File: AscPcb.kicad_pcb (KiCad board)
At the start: 2 copper layers, 36 parts, among them J1 12402012E212A, J2 B2B-PH-K-S, J3 Conn_01x10_Pin, SW1 RESET, SW1 TL3305AF260QG, SW2 BOOT, SW2 TL3305AF260QG, U1 ESP32-C3-WROOM-02-N4, U2 BQ24040DSQR, U3 TLV75801PDRVR

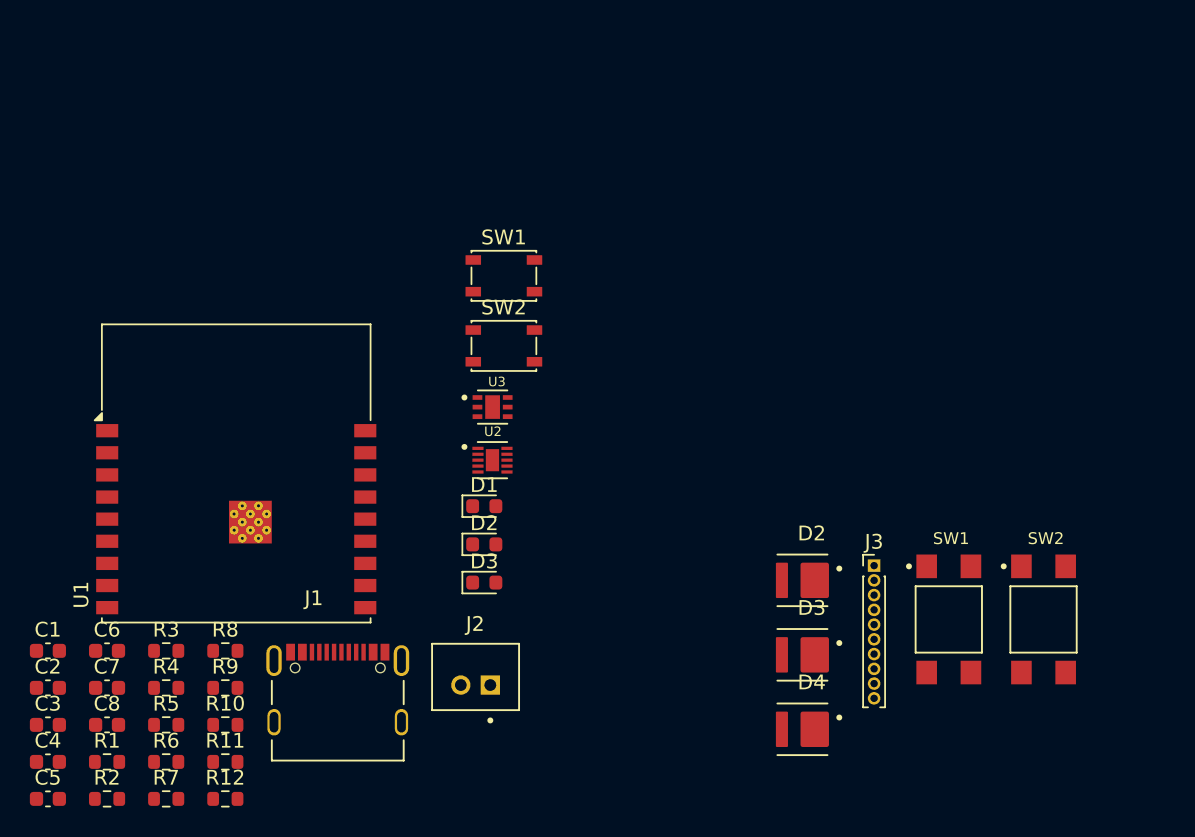
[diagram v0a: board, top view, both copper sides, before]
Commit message: sub circuits put together
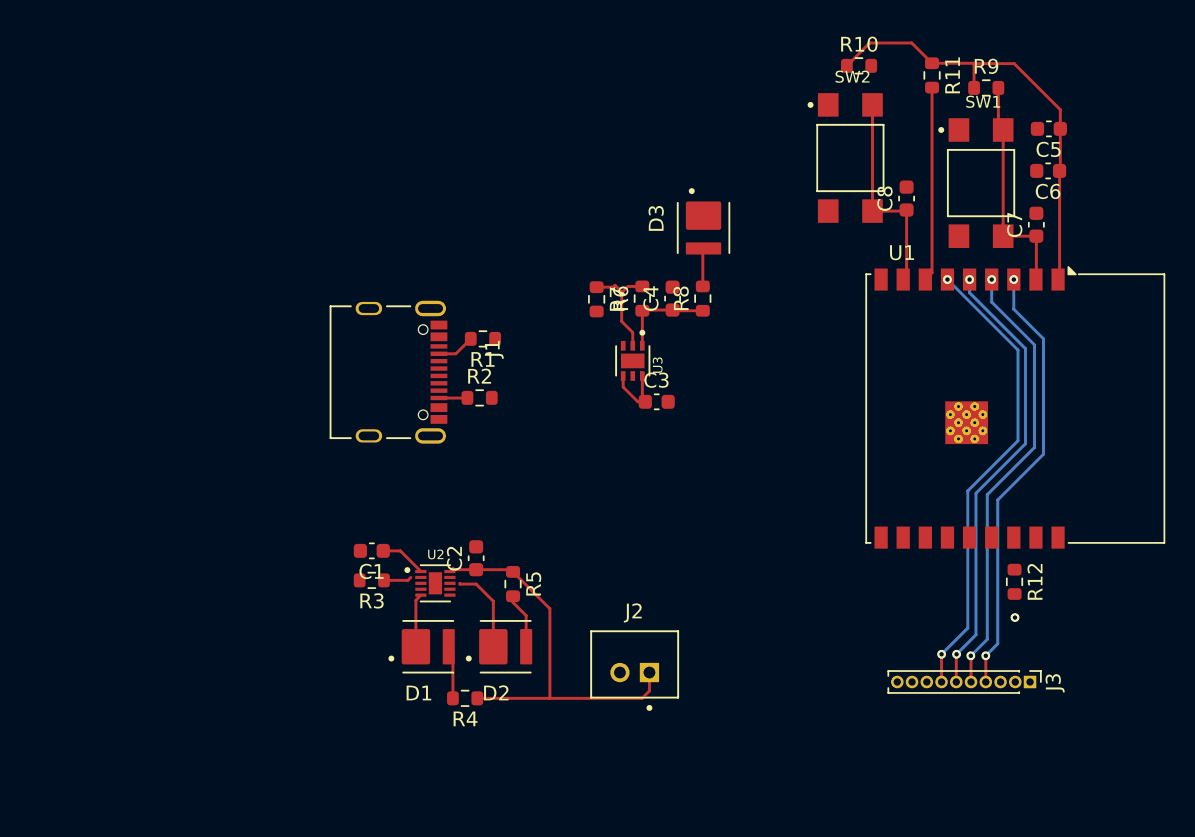
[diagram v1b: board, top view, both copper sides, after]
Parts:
- removed the D2 at (171.7, 106.9)
- removed the D2 at (150.1, 104.5)
- removed the D3 at (150.1, 107.0)
- removed the D3 at (171.7, 112.0)
- removed D4: Green, L135_G525003500000:LED_L135-G525003500000
- removed the SW1 at (151.4, 86.2)
- removed the SW1 at (181.6, 109.5)
- removed the SW2 at (151.4, 91.0)
- removed the SW2 at (188.0, 109.5)
- added D2: RED, L135_G525003500000:LED_L135-G525003500000, F.Cu at (151.5, 111.4)
- added D3: Green, L135_G525003500000:LED_L135-G525003500000, F.Cu at (165.0, 83.0)
- added SW1: TL3305AF260QG, TL3305AF260QG:SW_TL3305AF260QG, F.Cu at (183.8, 80.0)
- added SW2: TL3305AF260QG, TL3305AF260QG:SW_TL3305AF260QG, F.Cu at (174.9, 78.3)
- D1: footprint LED_SMD:LED_0603_1608Metric -> L135_G525003500000:LED_L135-G525003500000
- moved C5 81.7 mm to (188.4, 76.3), turned to 180 degrees
- moved C6 71.6 mm to (188.3, 79.1), turned to 180 degrees
- moved C7 70.4 mm to (187.5, 82.8), turned to 90 degrees
- moved R11 66.8 mm to (180.5, 72.7), turned to -90 degrees
- moved R9 65.7 mm to (184.1, 73.5)
- moved C8 64.9 mm to (178.7, 81.0), turned to 90 degrees
- moved R10 62.0 mm to (175.5, 72.0)
- moved R12 55.5 mm to (186.1, 107.0), turned to -90 degrees
- moved C4 52.7 mm to (162.9, 87.8), turned to 90 degrees
- moved U1 50.3 mm to (183.0, 95.2), turned to -90 degrees
- moved C3 46.7 mm to (161.8, 94.8)
- moved R6 45.1 mm to (160.8, 87.8), turned to 90 degrees
- moved R7 44.7 mm to (157.7, 87.8), turned to -90 degrees
- moved R8 40.2 mm to (164.9, 87.8), turned to 90 degrees
- moved R1 38.4 mm to (150.0, 90.5), turned to 180 degrees
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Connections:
- J3 pad 10: IO21 -> IO10
- J3 pad 8: IO10 -> IO21
- R4 pad 2: Net-(D4-PadA) -> Net-(D1-PadA)
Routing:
- net +3V3: track 0.00 -> 36.7 mm
- net POWER: track 0.00 -> 31.8 mm
- net IO7: track 0.00 -> 31.4 mm, vias 0 -> 2
- net IO6: track 0.00 -> 30.8 mm, vias 0 -> 2
- net IO5: track 0.00 -> 30.4 mm, vias 0 -> 2
- net IO4: track 0.00 -> 29.7 mm, vias 0 -> 2
- net Net-(U1-EN): track 0.00 -> 15.4 mm
- net Net-(U1-IO9): track 0.00 -> 14.4 mm
- net Net-(U1-IO8): track 0.00 -> 13.2 mm
- net Net-(U3-FB): track 0.00 -> 7.45 mm
- net Net-(U2-~{CHG}): track 0.00 -> 5.88 mm
- net Net-(D2-PadA): track 0.00 -> 3.79 mm
- net Net-(U2-~{PG}): track 0.00 -> 3.63 mm
- net Net-(D1-PadA): track 0.00 -> 3.62 mm
- net +5V: track 0.00 -> 3.13 mm
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
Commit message: connecting some more stuff
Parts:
- moved J2 1.19 mm to (161.5, 112.6)
- moved C2 1.19 mm to (150.7, 105.4)
- moved D1 1.19 mm to (147.5, 111.4)
- moved D2 1.19 mm to (152.7, 111.4)
- moved R4 1.19 mm to (150.0, 114.9)
- moved R5 1.19 mm to (153.2, 107.1)
- moved U2 1.19 mm to (148.0, 107.1)
- moved C1 1.19 mm to (143.7, 104.9)
- moved R3 1.19 mm to (143.7, 106.9)
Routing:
- net +3V3: track 36.7 -> 103.0 mm, vias 0 -> 2
- net D+: track 0.00 -> 50.4 mm, vias 0 -> 2
- net D-: track 0.00 -> 45.2 mm, vias 0 -> 3
- net IO0: track 0.00 -> 10.6 mm
- net IO1: track 0.00 -> 10.4 mm
- net IO10: track 0.00 -> 10.2 mm
- net IO20: track 0.00 -> 10.0 mm
- net IO21: track 0.00 -> 9.83 mm
- net Net-(U1-IO9): track 14.4 -> 17.0 mm
- net Net-(U1-IO2): track 0.00 -> 2.20 mm
- net (no net): vias 1 -> 0
- added copper zone on B.Cu, net GND
- added copper zone on F.Cu, net GND
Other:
- board outline added: 49.4 x 47.9 mm

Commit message: bad but working version of pcb
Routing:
- net +5V: track 3.13 -> 35.9 mm, vias 0 -> 2
- net POWER: track 31.8 -> 46.5 mm
- net GND: vias 0 -> 46

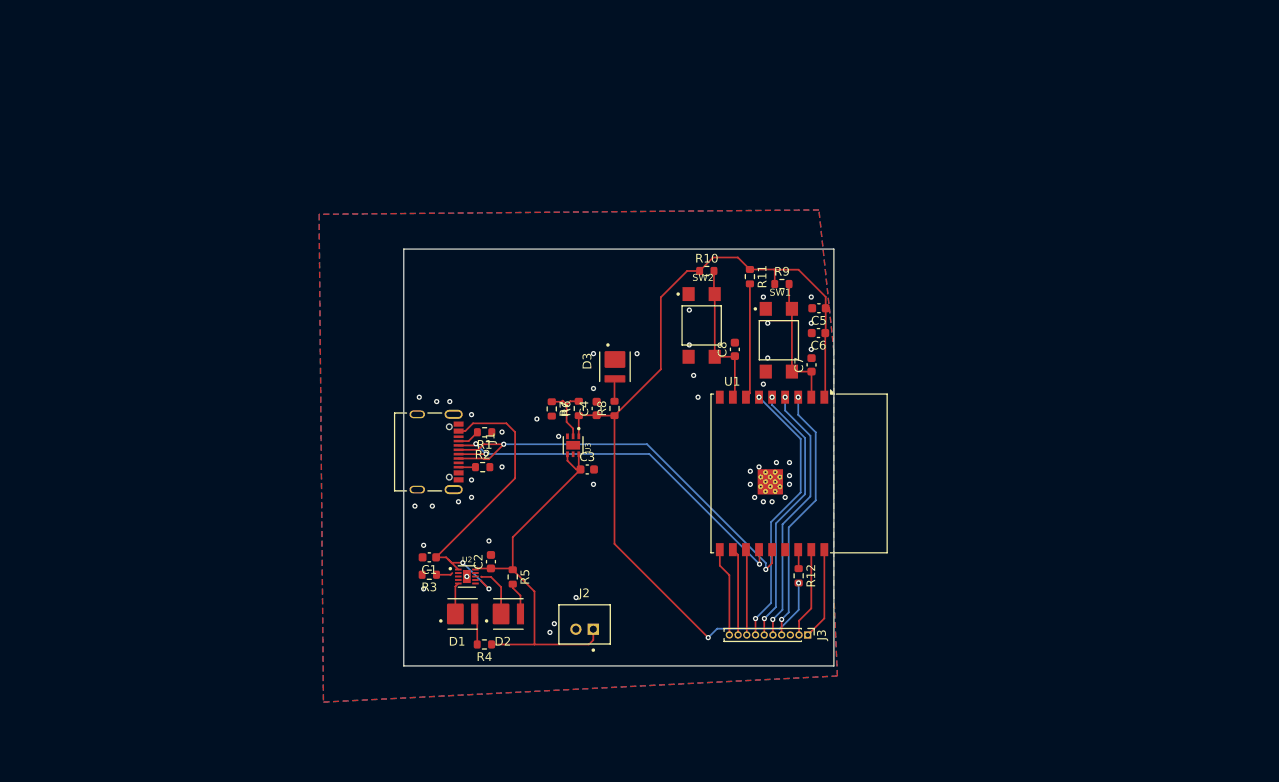
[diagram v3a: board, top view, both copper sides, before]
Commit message: new design: all components placed
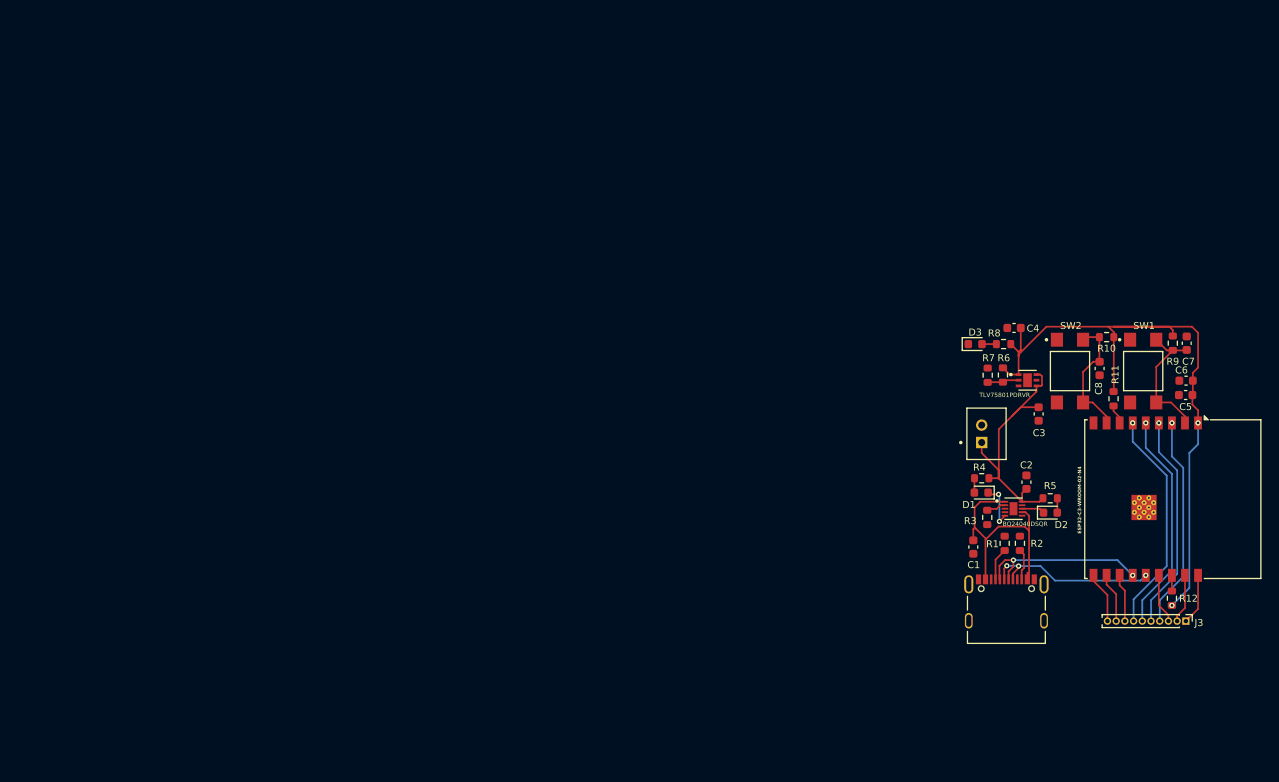
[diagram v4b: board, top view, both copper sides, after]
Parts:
- D1, D3: value Green -> GREEN; footprint L135_G525003500000:LED_L135-G525003500000 -> LED_SMD:LED_0603_1608Metric
- D2: footprint L135_G525003500000:LED_L135-G525003500000 -> LED_SMD:LED_0603_1608Metric
- J2: value B2B-PH-K-S -> B2B-PH-K-S(LF)(SN)
- R4, R5, R8: value 30 -> 150
- moved J1 70.4 mm to (209.9, 112.2), turned to 0 degrees
- moved R3 64.4 mm to (207.7, 100.3), turned to -90 degrees
- moved D2 63.3 mm to (214.9, 99.8), turned to 0 degrees
- moved U2 63.2 mm to (210.7, 99.3)
- moved C1 62.5 mm to (206.1, 103.7), turned to -90 degrees
- moved R5 62.4 mm to (214.9, 98.1), turned to 0 degrees
- moved R2 62.3 mm to (211.4, 103.3), turned to 90 degrees
- moved C2 62.1 mm to (212.2, 96.2)
- moved D1 61.1 mm to (207.0, 97.5)
- moved R1 61.0 mm to (209.7, 103.3), turned to -90 degrees
- moved R4 60.2 mm to (207.1, 95.8)
- moved U3 52.7 mm to (212.3, 84.5), turned to 0 degrees
- moved C3 52.2 mm to (213.6, 88.4), turned to -90 degrees
- moved J2 51.1 mm to (207.6, 90.7), turned to -90 degrees
- moved R7 50.2 mm to (207.8, 84.0), turned to 90 degrees
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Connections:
- R4 pad 2: Net-(D1-PadA) -> Net-(D1-A)
- R5 pad 2: Net-(D2-PadA) -> Net-(D2-A)
- R8 pad 2: Net-(D3-PadA) -> Net-(D3-A)
- U2 pad 5: Net-(U2-~{PG}) -> Net-(D1-K)
- U2 pad 8: Net-(U2-~{CHG}) -> Net-(D2-K)
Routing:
- net D+: track 50.4 -> 20.4 mm, vias 2 -> 3
- net D-: track 45.2 -> 20.3 mm, vias 3 -> 2
- net +3V3: track 103.0 -> 79.6 mm
- net POWER: track 46.5 -> 32.3 mm
- net Net-(U1-IO8): track 13.2 -> 2.24 mm
- net +5V: track 35.9 -> 29.0 mm, vias 2 -> 0
- net Net-(U2-~{CHG}): track 5.88 -> 0.00 mm
- net IO3: track 0.00 -> 5.71 mm
- net IO5: track 30.4 -> 24.9 mm, vias 2 -> 1
- net IO7: track 31.4 -> 25.9 mm, vias 2 -> 1
- net IO6: track 30.8 -> 25.4 mm, vias 2 -> 1
- net Net-(D1-K): track 0.00 -> 5.38 mm, vias 0 -> 2
- net IO4: track 29.7 -> 24.4 mm, vias 2 -> 1
- net IO1: track 10.4 -> 5.62 mm
- net IO0: track 10.6 -> 5.83 mm
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- removed copper zone on B.Cu, net GND
- removed copper zone on F.Cu, net GND
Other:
- board outline removed

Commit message: new version of pcb done
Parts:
- moved C6 82.0 mm to (149.7, 98.4)
- moved J1 82.0 mm to (129.1, 126.0)
- moved J2 82.0 mm to (126.8, 104.5)
- moved J3 82.0 mm to (149.7, 126.0)
- moved R10 82.0 mm to (140.6, 93.4)
- moved R12 82.0 mm to (148.1, 123.4)
- moved R5 82.0 mm to (134.1, 111.9)
- moved R6 82.0 mm to (128.7, 97.8)
- moved R9 82.0 mm to (148.2, 94.1)
- moved U1 82.0 mm to (145.1, 112.0)
- moved U2 82.0 mm to (129.9, 113.1)
- moved C1 82.0 mm to (125.3, 117.5)
- moved R4 82.0 mm to (126.2, 109.6)
- moved R7 82.0 mm to (126.9, 97.8)
- moved C2 82.0 mm to (131.4, 110.1)
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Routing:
- net +3V3: track 79.6 -> 70.1 mm
- net GND: vias 0 -> 41
- added copper zone on B.Cu, net GND
- added copper zone on F.Cu, net GND
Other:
- board outline added: 27.9 x 36.2 mm
- board text added: "0"
- board text added: "1"
- board text added: "10"
- board text added: "20"
- board text added: "21"
- board text added: "3"
- board text added: "4"
- board text added: "5"
- board text added: "6"
- board text added: "7"

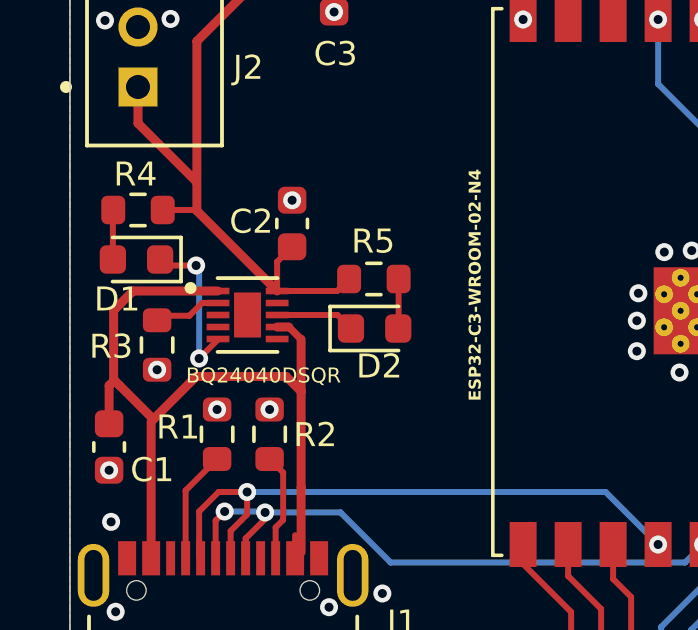
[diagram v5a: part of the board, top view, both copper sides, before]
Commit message: added bmi270 and ltc3625 and fixed some errors
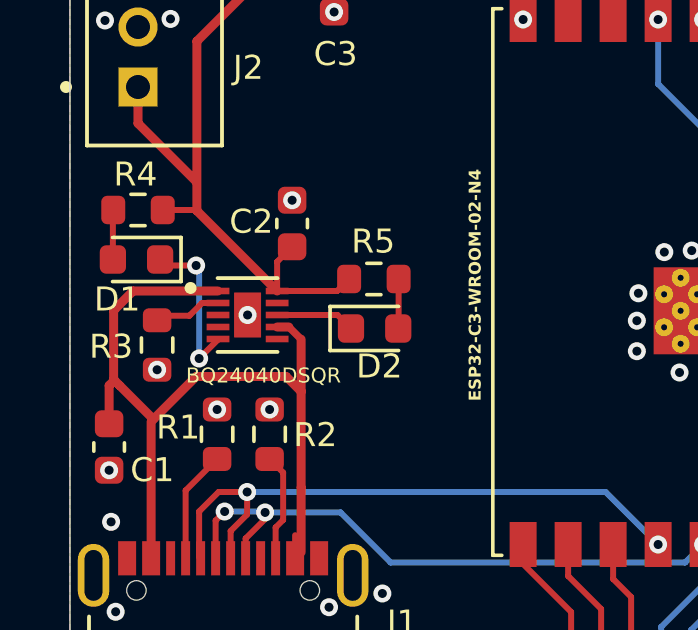
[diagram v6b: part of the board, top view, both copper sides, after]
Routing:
- net GND: vias 41 -> 42
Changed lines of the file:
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@@
+	)
+	(via
+		(at 129.873 113.1452)
+		(size 0.6)
+		(drill 0.3)
+		(layers "F.Cu" "B.Cu")
+		(net 1)
 	)
 	(via

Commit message: motor control circuit done
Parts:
- added C10: 220nF, Capacitor_SMD:C_0603_1608Metric, F.Cu at (148.5, 85.6)
- added C11: 100nF, Capacitor_SMD:C_0603_1608Metric, F.Cu at (148.5, 88.1)
- added C12: 22uF, Capacitor_SMD:C_0603_1608Metric, F.Cu at (148.5, 90.6)
- added C13: 22uF, Capacitor_SMD:C_0603_1608Metric, F.Cu at (148.5, 93.1)
- added C14: 10uF, Capacitor_SMD:C_0603_1608Metric, F.Cu at (148.5, 95.6)
- added C15: 100F, Capacitor_THT:CP_Radial_D22.0mm_P10.00mm_SnapIn, F.Cu at (108.3, 61.8)
- added C16: 100F, Capacitor_THT:CP_Radial_D22.0mm_P10.00mm_SnapIn, F.Cu at (108.3, 85.3)
- added C9: 10uF, Capacitor_SMD:C_0603_1608Metric, F.Cu at (148.5, 83.1)
- added D4: GREEN, LED_SMD:LED_0603_1608Metric, F.Cu at (118.8, 106.2)
- added D6: D_Schottky, Diode_SMD:D_SMA, F.Cu at (162.1, 71.0)
- added H1: MountingHole_Pad, MountingHole:MountingHole_3.2mm_M3_Pad, F.Cu at (129.0, 54.0)
- added H2: MountingHole_Pad, MountingHole:MountingHole_3.2mm_M3_Pad, F.Cu at (129.0, 61.9)
- added H3: MountingHole_Pad, MountingHole:MountingHole_3.2mm_M3_Pad, F.Cu at (129.0, 69.9)
- added H4: MountingHole_Pad, MountingHole:MountingHole_3.2mm_M3_Pad, F.Cu at (129.0, 77.8)
- added J4: Conn_01x06_Pin, Connector_PinHeader_2.54mm:PinHeader_1x06_P2.54mm_Vertical, F.Cu at (114.4, 99.4)
- added J5: Screw_Terminal_01x02, TerminalBlock_CUI:TerminalBlock_CUI_TB007-508-02_1x02_P5.08mm_Horizontal, F.Cu at (133.2, 87.7)
- added J6: Conn_01x02_Pin, Connector_PinHeader_2.54mm:PinHeader_1x02_P2.54mm_Vertical, F.Cu at (131.9, 109.2)
- added J7: Conn_01x02_Pin, Connector_PinHeader_2.54mm:PinHeader_1x02_P2.54mm_Vertical, F.Cu at (136.5, 109.2)
- added J8: Conn_01x03_Pin, Connector_PinHeader_2.54mm:PinHeader_1x03_P2.54mm_Vertical, F.Cu at (160.8, 84.1)
- added J9: Screw_Terminal_01x02, TerminalBlock_CUI:TerminalBlock_CUI_TB007-508-02_1x02_P5.08mm_Horizontal, F.Cu at (133.2, 100.3)
- added L1: 3.3uH, Inductor_SMD:L_0805_2012Metric, F.Cu at (140.0, 77.9)
- added L2: 3.3uH, DR73-3R3-R:DR73-3R3-R_EAT, F.Cu at (106.7, 101.7)
- added L3: 3.3uH, DR73-3R3-R:DR73-3R3-R_EAT, F.Cu at (106.7, 111.0)
- added Q1: Q_NMOS_DGS, DMN1019USN-13:SC-59-pads-swapped, F.Cu at (161.2, 77.6)
- added R13: 10k, Resistor_SMD:R_0603_1608Metric, F.Cu at (156.5, 88.1)
- added R14: 10k, Resistor_SMD:R_0603_1608Metric, F.Cu at (156.5, 90.6)
- added R15: 33.2k, Resistor_SMD:R_0805_2012Metric, F.Cu at (144.5, 78.0)
- added R16: 10k, Resistor_SMD:R_0603_1608Metric, F.Cu at (156.5, 93.1)
- added R17: 150, Resistor_SMD:R_0603_1608Metric, F.Cu at (156.5, 95.6)
- added R18: 61.9k, Resistor_SMD:R_0603_1608Metric, F.Cu at (156.5, 98.1)
- added U5: LTC3625EDE_PBF, LTC3625EDE_PBF:DFN-12_DE, F.Cu at (160.8, 94.2)
- added U6: BMI270, BMI270:XDCR_BMI270, F.Cu at (155.4, 113.4)
- added U8: AP62300TWU, Package_TO_SOT_SMD:TSOT-23-6, F.Cu at (161.1, 99.4)
- J3: footprint Connector_PinHeader_1.00mm:PinHeader_1x10_P1.00mm_Vertical -> Connector_PinHeader_2.54mm:PinHeader_1x10_P2.54mm_Vertical
- R6: value 10k -> 49.9k
- R7: value 49.9k -> 10k
- moved J3 47.5 mm to (127.3, 84.1), turned to 0 degrees
- moved U1 43.2 mm to (147.8, 68.9), turned to 0 degrees
- moved R3 40.3 mm to (152.5, 83.1), turned to 0 degrees
- moved C1 39.5 mm to (144.4, 83.1), turned to 0 degrees
- moved R12 38.8 mm to (156.5, 85.6), turned to 0 degrees
- moved R4 35.6 mm to (152.5, 85.6), turned to 0 degrees
- moved U2 35.2 mm to (135.6, 78.4)
- moved J1 34.4 mm to (158.4, 108.0)
- moved U3 32.4 mm to (160.3, 113.1)
- moved R5 30.1 mm to (152.5, 88.1)
- moved C2 27.8 mm to (144.4, 85.6), turned to 0 degrees
- moved R1 27.3 mm to (148.5, 98.1), turned to 0 degrees
- moved R7 26.0 mm to (152.5, 93.1), turned to 0 degrees
- moved R6 24.9 mm to (152.5, 90.6), turned to 0 degrees
- moved R2 24.3 mm to (148.5, 100.6), turned to 0 degrees
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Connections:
- C2 pad 1: POWER -> Net-(J6-Pin_2)
- J2 pad 1: POWER -> Net-(J6-Pin_2)
- R4 pad 1: POWER -> Net-(J6-Pin_2)
- R5 pad 1: POWER -> Net-(J6-Pin_2)
- U2 pad 10: POWER -> Net-(J6-Pin_2)
- U2 pad 3: unconnected-(U2-VSS-Pad3) -> GND
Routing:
- net +3V3: track 70.1 -> 0.00 mm, vias 2 -> 0
- net POWER: track 32.5 -> 0.00 mm
- net +5V: track 29.0 -> 0.00 mm
- net IO7: track 25.9 -> 0.00 mm, vias 1 -> 0
- net IO6: track 25.4 -> 0.00 mm, vias 1 -> 0
- net IO5: track 24.9 -> 0.00 mm, vias 1 -> 0
- net IO4: track 24.4 -> 0.00 mm, vias 1 -> 0
- net D+: track 20.4 -> 0.00 mm, vias 3 -> 0
- net D-: track 20.3 -> 0.00 mm, vias 2 -> 0
- net Net-(U1-EN): track 15.5 -> 0.00 mm
- net Net-(U1-IO9): track 14.8 -> 0.00 mm
- net IO10: track 5.91 -> 0.00 mm
- net IO0: track 5.83 -> 0.00 mm
- net IO20: track 5.71 -> 0.00 mm
- net IO3: track 5.71 -> 0.00 mm
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- removed copper zone on B.Cu, net GND
- removed copper zone on F.Cu, net GND
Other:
- board size 27.9 x 36.2 mm -> 73.4 x 73.8 mm
- board text removed: "0"
- board text removed: "1"
- board text removed: "10"
- board text removed: "20"
- board text removed: "21"
- board text removed: "3"
- board text removed: "4"
- board text removed: "5"
- board text removed: "6"
- board text removed: "7"
